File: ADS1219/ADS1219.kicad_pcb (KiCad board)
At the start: 2 copper layers, 25 x 25 mm, 19 parts, among them J1 qwiic, J2 Conn_01x06, J3 qwiic, J4 DRDY, U1 ADS1219IPW, U2 NCP51460SN33T1G

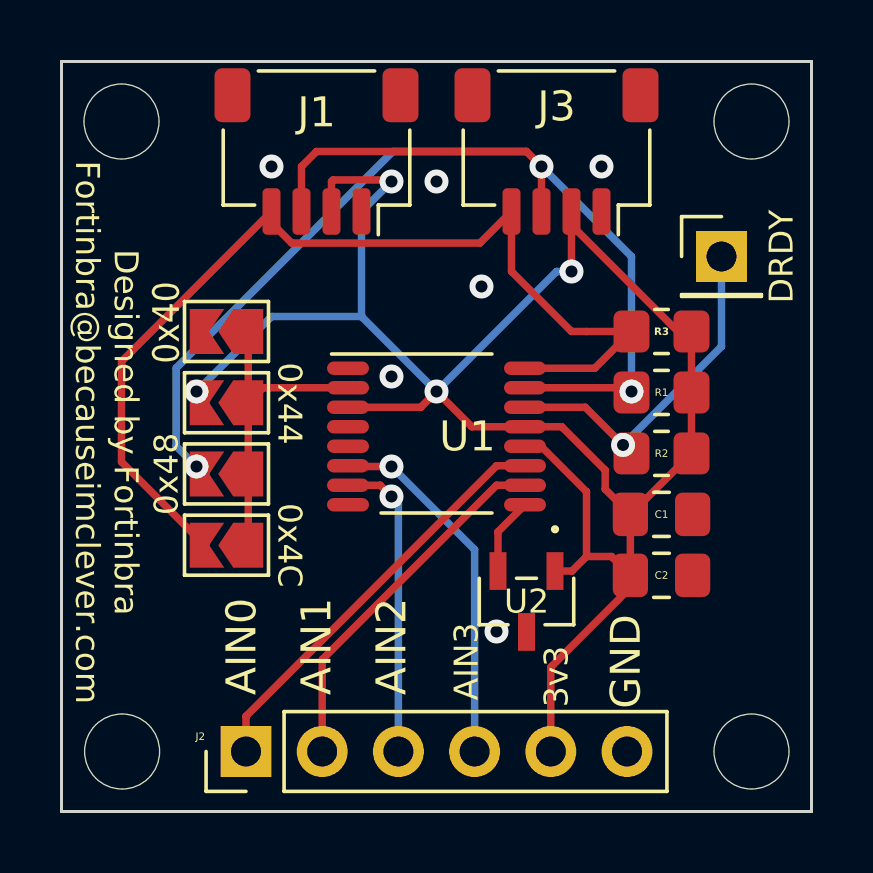
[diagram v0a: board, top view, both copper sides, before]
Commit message: Cleaning up ADS1219 board folders
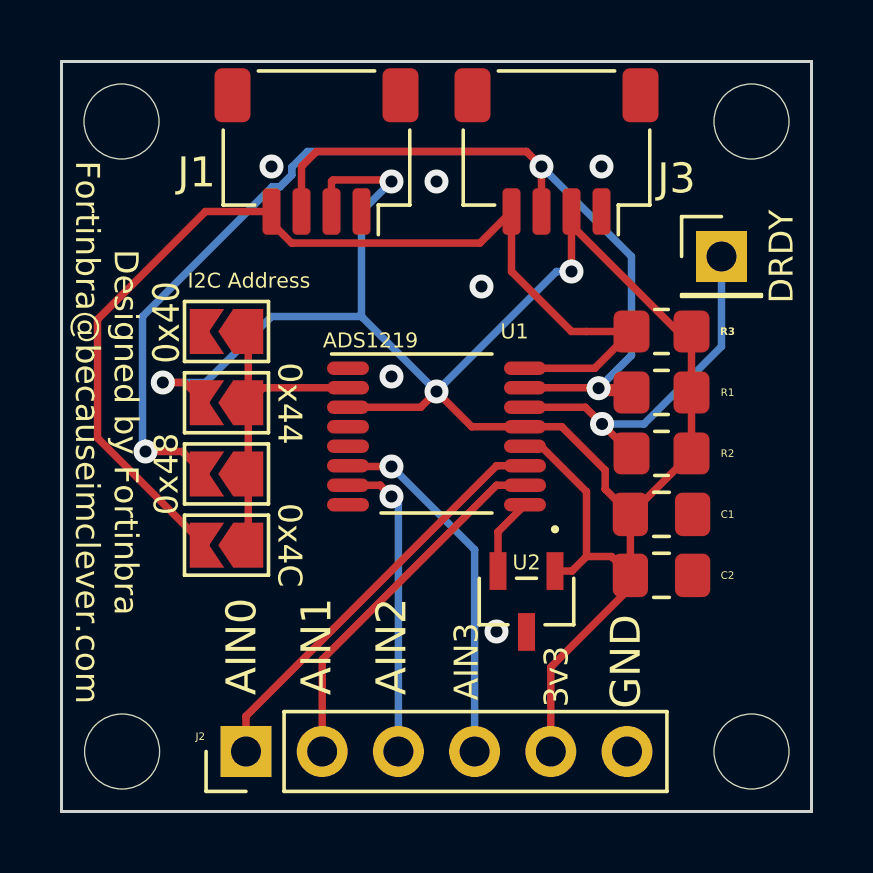
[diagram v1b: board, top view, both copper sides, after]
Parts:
- U1: value ADS1219IPW -> ADS1219
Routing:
- net /SDA: track 42.7 -> 48.0 mm
- net +3.3V: track 67.6 -> 70.2 mm
- net /SCL: track 34.3 -> 36.3 mm
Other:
- board text added: "I2C Address"

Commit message: add C3, 0.1uF decoupling cap for voltage reference IC - also rework board text labels
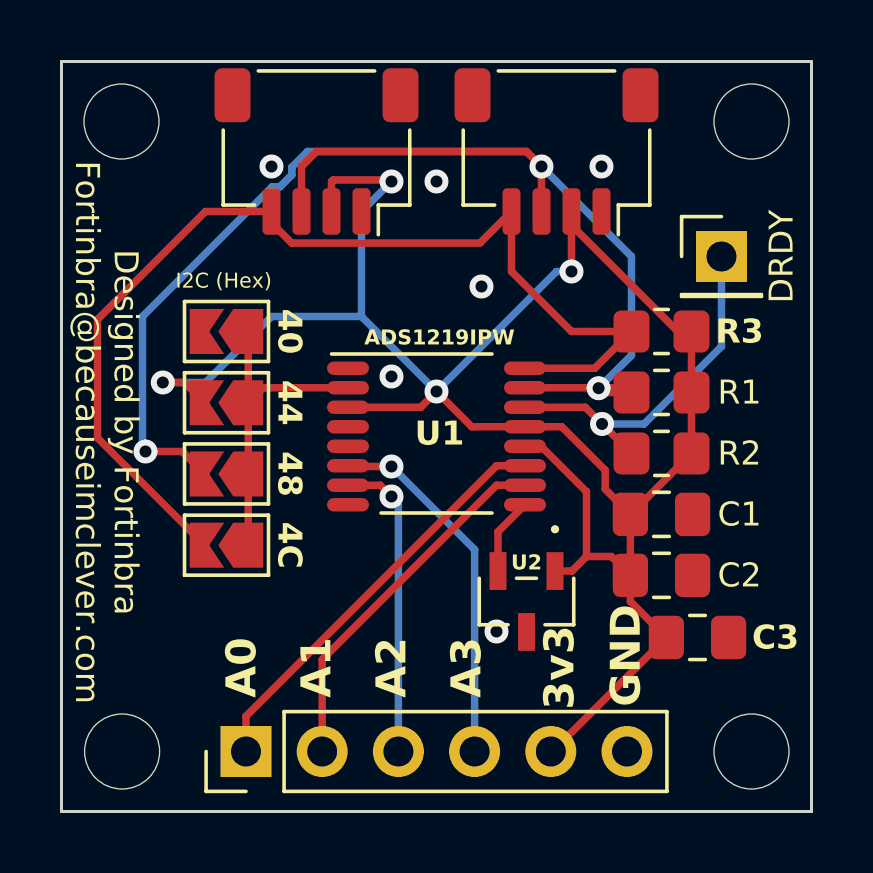
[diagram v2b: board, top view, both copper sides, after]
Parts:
- added C3: 0.1μF, Capacitor_SMD:C_0805_2012Metric_Pad1.18x1.45mm_HandSolder, F.Cu at (179.2, 93.2)
- C2: value 0.1μf -> 0.1μF
- U1: value ADS1219 -> ADS1219IPW
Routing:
- net +3.3V: track 70.2 -> 71.3 mm
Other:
- board text added: "A0"
- board text added: "A1"
- board text added: "A2"
- board text added: "A3"
- board text added: "I2C (Hex)"
- board text removed: "AIN0"
- board text removed: "AIN1"
- board text removed: "AIN2"
- board text removed: "AIN3"
- board text removed: "I2C Address"
